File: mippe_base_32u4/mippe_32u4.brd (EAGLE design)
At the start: 160 x 100 mm, 27 parts, among them J2 USB, SW1 BTN-PTS810, U1 ATMEGA32U4-XUMU, U2 AZ1117EH-3.3TRG1, Y1 16MHz

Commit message: Progress on layout
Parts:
- removed C12, C8: 1uF, scono:0603-CAP
- removed U2: AZ1117EH-3.3TRG1, scono:SOT230P700X180-4N
- U1: device SmartPrj:QFN44ML7X7 -> scono:QFN44ML7X7
- Z1, Z2: device varistor:CT/CN0603 -> scono:0603-RES
- moved Y1 130.8 mm to (27.5, 21.8), flipped to the bottom, turned to 270 degrees
- moved C3 129.1 mm to (27.5, 26.8), flipped to the bottom
- moved C4 124.8 mm to (27.8, 17.0), flipped to the bottom
- moved F1 124.4 mm to (13.0, 6.00), turned to 270 degrees
- moved SW1 123.9 mm to (19.2, 32.0), turned to 180 degrees
- moved J2 120.5 mm to (19.2, 2.75)
- moved C1 118.0 mm to (28.5, 22.0), turned to 270 degrees
- moved R2 111.4 mm to (26.2, 17.8), turned to 270 degrees
- moved C2 109.6 mm to (24.0, 10.8), turned to 270 degrees
- moved C5 107.8 mm to (26.2, 22.0), turned to 270 degrees
- moved R1 103.6 mm to (11.8, 26.2), turned to 270 degrees
- moved C11 99.7 mm to (26.8, 8.75), turned to 90 degrees
- moved C6 95.7 mm to (11.8, 17.8), turned to 90 degrees
- moved D1 94.5 mm to (28.8, 3.75), turned to 270 degrees
- moved L3 93.1 mm to (24.5, 6.75), turned to 90 degrees
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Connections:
- removed net 3.3V: C12.2, U2.2, U2.4
- net 5V: no longer C8.2, U2.3
- net GND: no longer C12.1, C8.1, U2.1
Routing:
- net 5V: track 0.00 -> 3.15 mm, vias 0 -> 1
- added copper zone on layer 16, net 5V
- added copper zone on layer 1, net GND

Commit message: blah
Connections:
- net D+ renamed D_P
- net D- renamed D_N
- net RD+ renamed RD_P
- net RD- renamed RD_N
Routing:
- net 5V: track 3.15 -> 29.7 mm, vias 1 -> 11
- net RD_P: track 0.00 -> 7.64 mm
- net RD_N: track 0.00 -> 7.62 mm
- net AGND: track 0.00 -> 7.51 mm
- net D_P: track 0.00 -> 7.20 mm
- net D_N: track 0.00 -> 6.88 mm
- net HWB: track 0.00 -> 6.03 mm
- net AREF: track 0.00 -> 5.01 mm
- net UGND: track 0.00 -> 3.70 mm, vias 0 -> 1
- net UCAP: track 0.00 -> 2.65 mm, vias 0 -> 1

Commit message: layout more
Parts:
- added D2, D3: (no value), scono:LED-0603
- added J1, J4: i2c, scono:1X02
- added J3: spi, scono:1X03
- added J5: BURNIN, scono:BURNIN
- added R3, R7: 330R, scono:0603-RES
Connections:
- new net N$1: D2.C, R3.2
- new net N$2: D3.C, R7.2
- net 5V: now also D2.A, D3.A
- net D0/RX: now also J4.1
- net D1/TX: now also J4.2
- net D2/SDA: now also J1.2
- net D3/SCL: now also J1.1
- net MISO: now also J3.3
- net MOSI: now also J3.2
- net RXLED: now also R7.1
- net SCK: now also J3.1
- net TXLED: now also R3.1
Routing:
- net RESET: track 0.00 -> 27.3 mm, vias 0 -> 2
- net GND: track 0.00 -> 23.6 mm, vias 0 -> 4
- net RXLED: track 0.00 -> 18.9 mm, vias 0 -> 2
- net UGND: track 3.70 -> 21.5 mm
- net SHIELD: track 0.00 -> 16.2 mm
- net SCK: track 0.00 -> 16.0 mm
- net MOSI: track 0.00 -> 14.4 mm
- net D3/SCL: track 0.00 -> 13.1 mm, vias 0 -> 1
- net MISO: track 0.00 -> 13.0 mm
- net D2/SDA: track 0.00 -> 11.6 mm
- net D1/TX: track 0.00 -> 11.1 mm
- net D0/RX: track 0.00 -> 11.0 mm
- net UCAP: track 2.65 -> 12.9 mm
- net XTAL1: track 0.00 -> 9.02 mm, vias 0 -> 1
- net XTAL2: track 0.00 -> 8.61 mm, vias 0 -> 1
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
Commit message: finish 32u4 and rev c burnin
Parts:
- added D4: (no value), scono:LED-0603
- added J6: GND, scono:1X02
- added J7: VCC, scono:1X02
- added R8: 330R, scono:0603-RES
- J4: value i2c -> UART
- moved J1 7.62 mm to (25.4, 17.8)
- moved J3 7.62 mm to (25.4, 10.2)
- moved J4 7.62 mm to (25.4, 22.9)
- moved C1 7.50 mm to (21.0, 22.0)
- moved C11 7.50 mm to (19.2, 8.75)
- moved C2 7.50 mm to (16.5, 10.8)
- moved C3 7.50 mm to (20.0, 26.8)
- moved C4 7.50 mm to (20.2, 17.0)
- moved C5 7.50 mm to (18.8, 22.0)
- moved C6 7.50 mm to (4.25, 17.8)
- moved D2 7.50 mm to (19.3, 32.2)
- moved F1 7.50 mm to (5.50, 6.00)
- moved J2 7.50 mm to (11.8, 2.75)
- moved J5 7.50 mm to (15.5, 32.0)
- moved L2 7.50 mm to (4.25, 14.0)
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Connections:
- new net N$4: D4.C, R8.2
- net 5V: now also J5.3.3V, J7.1, J7.2
- net D7: now also D4.A
- net GND: now also J5.GND, J6.1, J6.2, R8.1
- net MISO: now also J5.MISO
- net MOSI: now also J5.MOSI
- net RESET: now also J5.RST
- net SCK: now also J5.SCK
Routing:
- net SCK: track 16.0 -> 38.2 mm, vias 0 -> 1
- net MISO: track 13.0 -> 33.5 mm, vias 0 -> 1
- net MOSI: track 14.4 -> 33.0 mm, vias 0 -> 1
- net N$3: track 2.01 -> 6.47 mm
- net N$4: track 0.00 -> 3.64 mm
- net D7: track 0.00 -> 3.28 mm
- net RESET: track 27.3 -> 29.8 mm, vias 2 -> 3
- net GND: track 23.6 -> 25.0 mm, vias 4 -> 5
- net 5V: track 33.7 -> 34.5 mm
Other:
- board size 160 x 100 mm -> 28 x 36 mm
- board text added: "Arias Research Group"
- board text added: "Design by Seiya Fa'19"

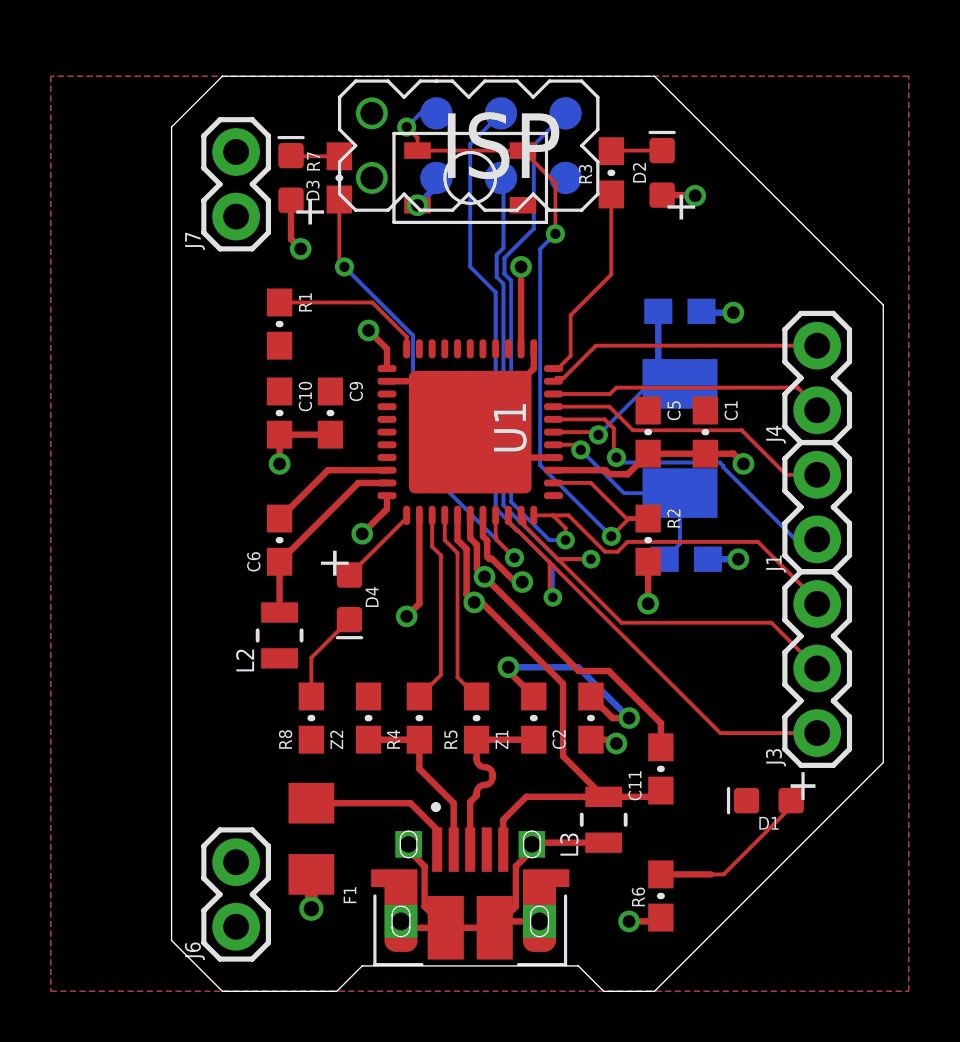
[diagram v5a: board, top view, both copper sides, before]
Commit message: Add same pinpouts as mipp_v2
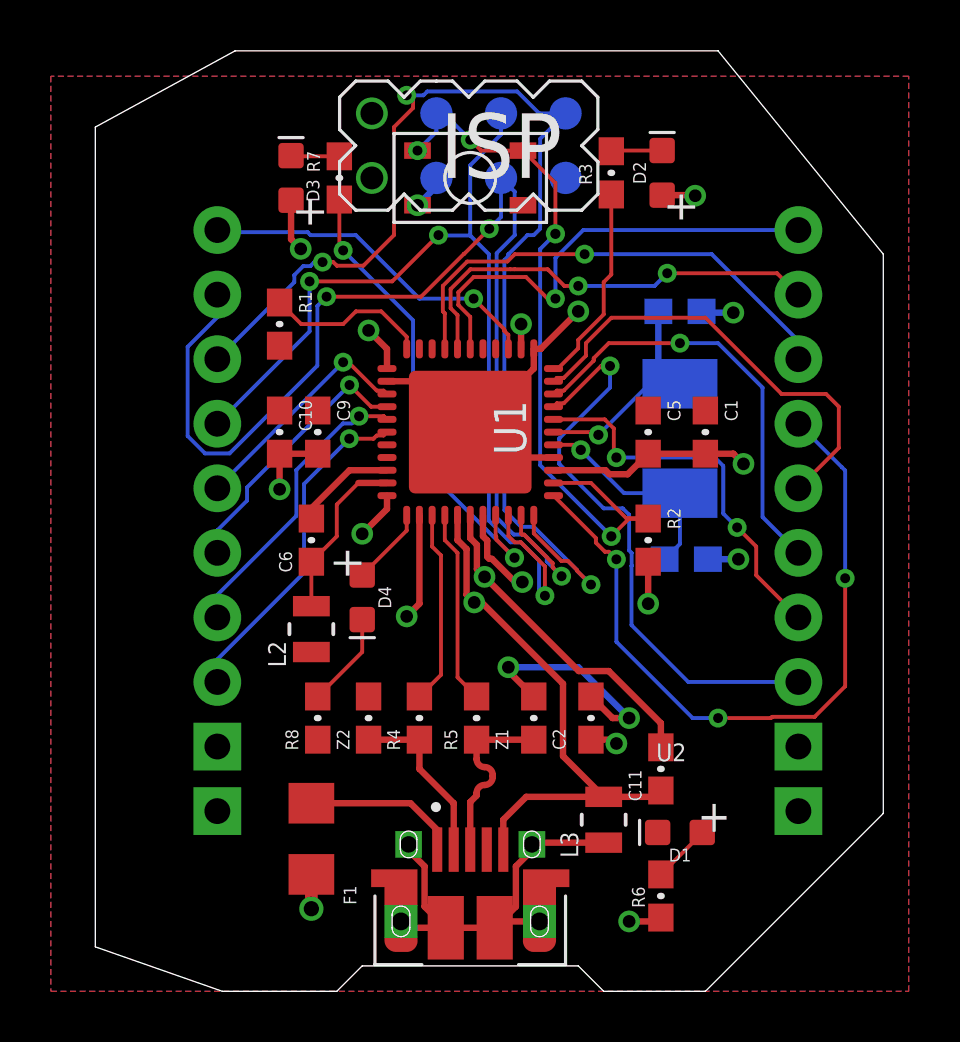
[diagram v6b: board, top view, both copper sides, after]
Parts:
- removed J1: i2c, scono:1X02
- removed J3: spi, scono:1X03
- removed J4: UART, scono:1X02
- removed J6: GND, scono:1X02
- removed J7: VCC, scono:1X02
- added U2: MIPPE, scono:MIPPE
- moved D1 3.72 mm to (20.0, 6.25)
- moved L2 1.27 mm to (5.50, 14.2)
- moved C6 1.25 mm to (5.50, 17.8)
- moved C9 0.90 mm to (5.75, 22.0)
- moved C10 0.75 mm to (4.25, 22.0)
- moved D4 0.50 mm to (7.50, 15.5)
- moved R8 0.25 mm to (5.75, 10.8)
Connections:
- net 5V: now also U2.VCC, U2.VCC@1; no longer J7.1, J7.2
- net A0: now also U2.ADC0
- net A1: now also U2.ADC1
- net A2: now also U2.ADC2
- net A3: now also U2.ADC3
- net D0/RX: now also U2.RX; no longer J4.1
- net D1/TX: now also U2.TX; no longer J4.2
- net D2/SDA: now also U2.SDA; no longer J1.2
- net D3/SCL: now also U2.SCL; no longer J1.1
- net D4: now also U2.SS
- net GND: now also U2.GND@0, U2.GND@1; no longer J6.1, J6.2
- net IO10*: now also U2.GPIO5
- net IO11*: now also U2.GPIO6
- net IO8: now also U2.GPIO3
- net IO9*: now also U2.GPIO4
- net MISO: now also U2.MISO; no longer J3.3
- net MOSI: now also U2.MOSI; no longer J3.2
- net SCK: now also U2.SCK; no longer J3.1
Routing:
- net IO11*: track 0.00 -> 28.7 mm, vias 0 -> 3
- net IO10*: track 0.00 -> 19.1 mm, vias 0 -> 1
- net IO8: track 0.00 -> 18.5 mm, vias 0 -> 1
- net IO9*: track 0.00 -> 17.3 mm, vias 0 -> 2
- net D4: track 0.00 -> 13.7 mm, vias 0 -> 1
- net MISO: track 33.5 -> 47.0 mm, vias 1 -> 3
- net A3: track 0.00 -> 13.3 mm, vias 0 -> 1
- net MOSI: track 33.0 -> 46.0 mm, vias 1 -> 3
- net A2: track 0.00 -> 11.6 mm, vias 0 -> 1
- net D2/SDA: track 11.5 -> 23.0 mm, vias 0 -> 1
- net A1: track 0.00 -> 10.6 mm, vias 0 -> 1
- net A0: track 0.00 -> 9.25 mm, vias 0 -> 1
- net D1/TX: track 11.0 -> 17.9 mm
- net D0/RX: track 10.9 -> 16.9 mm, vias 0 -> 1
- net N$3: track 6.47 -> 2.32 mm
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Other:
- board size 28 x 36 mm -> 31 x 37 mm

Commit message: Add files for jlc order
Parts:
- moved C1 3.00 mm to (24.0, 22.0)
- moved C10 3.00 mm to (7.25, 22.0)
- moved C11 3.00 mm to (22.2, 8.75)
- moved C2 3.00 mm to (19.5, 10.8)
- moved C3 3.00 mm to (23.0, 26.8)
- moved C4 3.00 mm to (23.2, 17.0)
- moved C5 3.00 mm to (21.8, 22.0)
- moved C6 3.00 mm to (8.50, 17.8)
- moved C9 3.00 mm to (8.75, 22.0)
- moved D1 3.00 mm to (23.0, 6.25)
- moved D2 3.00 mm to (22.3, 32.2)
- moved D3 3.00 mm to (7.70, 32.0)
- moved D4 3.00 mm to (10.5, 15.5)
- moved F1 3.00 mm to (8.50, 6.00)
- moved J2 3.00 mm to (14.8, 2.75)
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
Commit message: update jlc drc
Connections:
- removed net UGND: C11.1, J2.5, L3.2, U1.5
- net GND: now also C11.1, J2.5, L3.2, U1.5
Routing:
- net GND: track 27.3 -> 56.2 mm, vias 6 -> 7
- net UGND: track 21.5 -> 0.00 mm, vias 1 -> 0
- net 5V: track 32.0 -> 33.0 mm
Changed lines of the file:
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@@
 <?xml version="1.0" encoding="utf-8"?>
 <!DOCTYPE eagle SYSTEM "eagle.dtd">
-<eagle version="9.5.1">
+<eagle version="9.5.2">
 <drawing>
 <settings>
@@
 </variantdefs>
 <classes>
-<class number="0" name="default" width="0.1524" drill="0.381">
-<clearance class="0" value="0.1524"/>
+<class number="0" name="default" width="0.0889" drill="0.2">
+<clearance class="0" value="0.1397"/>
 </class>
-<class number="1" name="power" width="0.254" drill="0.499">
-<clearance class="0" value="0.1524"/>
-<clearance class="1" value="0.254"/>
-</class>
-<class number="2" name="gnd" width="0.254" drill="0.499">
-<clearance class="0" value="0.1524"/>
+<class number="2" name="gnd" width="0.0889" drill="0.2">
 <clearance class="1" value="0.1524"/>
-<clearance class="2" value="0.254"/>
-</class>
-<class number="3" name="usbvcc" width="0.254" drill="0.499">
-<clearance class="0" value="0.1524"/>
-<clearance class="1" value="0.1524"/>
-<clearance class="2" value="0.1524"/>
-<clearance class="3" value="0.254"/>
-</class>
-<class number="4" name="aref" width="0.254" drill="0.499">
-<clearance class="0" value="0.1524"/>
-<clearance class="1" value="0.1524"/>
-<clearance class="2" value="0.1524"/>
-<clearance class="3" value="0.1524"/>
-<clearance class="4" value="0.254"/>
-</class>
-<class number="5" name="diff pairs" width="0.1524" drill="0">
-<clearance class="0" value="0.1524"/>
-<clearance class="1" value="0.1524"/>
-<clearance class="2" value="0.1524"/>
-<clearance class="3" value="0.1524"/>
-<clearance class="4" value="0.1524"/>
-<clearance class="5" value="0.1524"/>
+<clearance class="2" value="0.1397"/>
 </class>
 </classes>
@@
 </elements>
 <signals>
-<signal name="GND" class="2">
+<signal name="GND">
 <contactref element="U1" pad="15"/>
 <contactref element="U1" pad="23"/>
@@
 <wire x1="17.525" y1="25.275" x2="19" y2="26.75" width="0.254" layer="1"/>
 <via x="19" y="26.75" extent="1-16" drill="0.499"/>
-</signal>
-<signal name="N$3">
-<contactref element="R6" pad="1"/>
-<contactref element="D1" pad="A"/>
-<wire x1="22.25" y1="4.6" x2="23.877" y2="6.227" width="0.1524" layer="1"/>
-<wire x1="23.877" y1="6.227" x2="23.877" y2="6.25" width="0.1524" layer="1"/>
-</signal>
-<signal name="D_N" class="5">
-<contactref element="Z2" pad="1"/>
-<contactref element="R4" pad="1"/>
-<contactref element="J2" pad="2"/>
-<wire x1="10.75" y1="9.9" x2="12.75" y2="9.9" width="0.254" layer="1"/>
-<wire x1="14.1" y1="5.575" x2="14.1" y2="7.4" width="0.254" layer="1"/>
-<wire x1="12.75" y1="8.75" x2="12.75" y2="9.9" width="0.254" layer="1"/>
-<wire x1="12.75" y1="8.75" x2="14.1" y2="7.4" width="0.254" layer="1"/>
-</signal>
-<signal name="D_P" class="5">
-<contactref element="Z1" pad="1"/>
-<contactref element="R5" pad="1"/>
-<contactref element="J2" pad="3"/>
-<wire x1="15" y1="9.9" x2="17.25" y2="9.9" width="0.254" layer="1"/>
-<wire x1="15" y1="9.9" x2="15" y2="9.1393625" width="0.254" layer="1"/>
-<wire x1="15" y1="9.1393625" x2="15.3175" y2="8.8218625" width="0.254" layer="1" curve="90"/>
-<wire x1="15.3175" y1="8.8218625" x2="15.635" y2="8.5043625" width="0.254" layer="1" curve="-90"/>
-<wire x1="15.635" y1="8.5043625" x2="15.635" y2="8.435" width="0.254" layer="1"/>
-<wire x1="15.635" y1="8.435" x2="15.3175" y2="8.1175" width="0.254" layer="1" curve="-90"/>
-<wire x1="15.3175" y1="8.1175" x2="15" y2="7.8" width="0.254" layer="1" curve="90"/>
-<wire x1="15" y1="7.8" x2="15" y2="7.7" width="0.254" layer="1"/>
-<wire x1="14.75" y1="5.575" x2="14.75" y2="7.45" width="0.254" layer="1"/>
-<wire x1="15" y1="7.7" x2="14.75" y2="7.45" width="0.254" layer="1"/>
-</signal>
-<signal name="UGND" class="2">
 <contactref element="U1" pad="5"/>
 <contactref element="C11" pad="1"/>
@@
 <wire x1="18.4" y1="12.1" x2="15.2" y2="15.3" width="0.254" layer="1"/>
 <wire x1="15.2" y1="15.3" x2="14.9059" y2="15.3" width="0.254" layer="1"/>
+<wire x1="22.25" y1="7.9" x2="22.25" y2="6.377" width="0.254" layer="1"/>
+<wire x1="22.25" y1="6.377" x2="22.123" y2="6.25" width="0.254" layer="1"/>
+<wire x1="22.25" y1="7.9" x2="22.4" y2="7.75" width="0.254" layer="1"/>
+<wire x1="27" y1="7.75" x2="27.66" y2="7.09" width="0.254" layer="1"/>
+<wire x1="22.4" y1="7.75" x2="27" y2="7.75" width="0.254" layer="1"/>
+<wire x1="24" y1="22.85" x2="23.85" y2="26.75" width="0" layer="19" extent="1-16"/>
+<wire x1="21.75" y1="22.85" x2="24" y2="22.85" width="0" layer="19" extent="1-1"/>
+<wire x1="18.025" y1="21" x2="21.75" y2="22.85" width="0" layer="19" extent="1-1"/>
+<wire x1="8.75" y1="22.85" x2="11.475" y2="24" width="0" layer="19" extent="1-1"/>
+<wire x1="7.25" y1="22.85" x2="8.75" y2="22.85" width="0" layer="19" extent="1-1"/>
+<wire x1="7.25" y1="25.4" x2="7.25" y2="22.85" width="0" layer="19" extent="1-1"/>
+<wire x1="14.25" y1="18.725" x2="14.75" y2="22" width="0" layer="19" extent="1-1"/>
+<wire x1="27.66" y1="9.63" x2="27.66" y2="7.09" width="0" layer="19" extent="1-1"/>
+<wire x1="16.25" y1="12.75" x2="14.9059" y2="15.3" width="0" layer="19" extent="1-1"/>
+<wire x1="16.825" y1="30.925" x2="19" y2="26.75" width="0" layer="19" extent="1-1"/>
+<wire x1="13.42" y1="32" x2="16.825" y2="30.925" width="0" layer="19" extent="1-16"/>
+<wire x1="10.75" y1="11.6" x2="14.9059" y2="15.3" width="0" layer="19" extent="1-1"/>
+<wire x1="8.75" y1="9.9" x2="10.75" y2="11.6" width="0" layer="19" extent="1-1"/>
+<wire x1="8.5" y1="13.3484" x2="10.75" y2="11.6" width="0" layer="19" extent="1-1"/>
+<wire x1="24.1" y1="17" x2="24" y2="22.85" width="0" layer="19" extent="1-16"/>
+</signal>
+<signal name="N$3">
+<contactref element="R6" pad="1"/>
+<contactref element="D1" pad="A"/>
+<wire x1="22.25" y1="4.6" x2="23.877" y2="6.227" width="0.1524" layer="1"/>
+<wire x1="23.877" y1="6.227" x2="23.877" y2="6.25" width="0.1524" layer="1"/>
+</signal>
+<signal name="D_N">
+<contactref element="Z2" pad="1"/>
+<contactref element="R4" pad="1"/>
+<contactref element="J2" pad="2"/>
+<wire x1="10.75" y1="9.9" x2="12.75" y2="9.9" width="0.254" layer="1"/>
+<wire x1="14.1" y1="5.575" x2="14.1" y2="7.4" width="0.254" layer="1"/>
+<wire x1="12.75" y1="8.75" x2="12.75" y2="9.9" width="0.254" layer="1"/>
+<wire x1="12.75" y1="8.75" x2="14.1" y2="7.4" width="0.254" layer="1"/>
+</signal>
+<signal name="D_P">
+<contactref element="Z1" pad="1"/>
+<contactref element="R5" pad="1"/>
+<contactref element="J2" pad="3"/>
+<wire x1="15" y1="9.9" x2="17.25" y2="9.9" width="0.254" layer="1"/>
+<wire x1="15" y1="9.9" x2="15" y2="9.1393625" width="0.254" layer="1"/>
+<wire x1="15" y1="9.1393625" x2="15.3175" y2="8.8218625" width="0.254" layer="1" curve="90"/>
+<wire x1="15.3175" y1="8.8218625" x2="15.635" y2="8.5043625" width="0.254" layer="1" curve="-90"/>
+<wire x1="15.635" y1="8.5043625" x2="15.635" y2="8.435" width="0.254" layer="1"/>
+<wire x1="15.635" y1="8.435" x2="15.3175" y2="8.1175" width="0.254" layer="1" curve="-90"/>
+<wire x1="15.3175" y1="8.1175" x2="15" y2="7.8" width="0.254" layer="1" curve="90"/>
+<wire x1="15" y1="7.8" x2="15" y2="7.7" width="0.254" layer="1"/>
+<wire x1="14.75" y1="5.575" x2="14.75" y2="7.45" width="0.254" layer="1"/>
+<wire x1="15" y1="7.7" x2="14.75" y2="7.45" width="0.254" layer="1"/>
 </signal>
 <signal name="XUSB">
@@
 <wire x1="13.45" y1="6.35" x2="12.4" y2="7.4" width="0.254" layer="1"/>
 </signal>
-<signal name="AREF" class="4">
+<signal name="AREF">
 <contactref element="U1" pad="42"/>
 <contactref element="C6" pad="2"/>
@@
 <wire x1="20" y1="26.62965625" x2="20" y2="27.9" width="0.1524" layer="1"/>
 </signal>
-<signal name="5V" class="1">
+<signal name="5V">
 <contactref element="U1" pad="7"/>
 <contactref element="C10" pad="2"/>
@@
 <wire x1="7.25" y1="21.15" x2="7.25" y2="19.75" width="0.254" layer="1"/>
 <via x="7.25" y="19.75" extent="1-16" drill="0.499"/>
-<wire x1="16.75" y1="25.275" x2="16.75" y2="26.25" width="0.254" layer="1"/>
-<via x="16.75" y="26.25" extent="1-16" drill="0.499"/>
+<wire x1="16.75" y1="25.275" x2="16.75" y2="27.25" width="0.254" layer="1"/>
+<via x="16.75" y="27.25" extent="1-16" drill="0.499"/>
+<wire x1="18.5" y1="32" x2="22.3" y2="31.323" width="0" layer="19" extent="1-16"/>
+<wire x1="16.75" y1="27.25" x2="18.5" y2="32" width="0" layer="19" extent="16-16"/>
+<wire x1="18.025" y1="20.5" x2="16.75" y2="25.275" width="0" layer="19" extent="1-1"/>
+<wire x1="15.25" y1="18.725" x2="18.025" y2="20.5" width="0" layer="19" extent="1-1"/>
+<wire x1="12.75" y1="18.725" x2="15.25" y2="18.725" width="0" layer="19" extent="1-1"/>
+<wire x1="11.475" y1="19.5" x2="12.75" y2="18.725" width="0" layer="19" extent="1-1"/>
+<wire x1="8.75" y1="21.15" x2="11.475" y2="19.5" width="0" layer="19" extent="1-1"/>
+<wire x1="21.75" y1="16.9" x2="21.75" y2="21.15" width="0" layer="19" extent="1-1"/>
+<wire x1="11.475" y1="24.5" x2="8.75" y2="21.15" width="0" layer="19" extent="1-1"/>
+<wire x1="8.08" y1="29.21" x2="10.75" y2="26" width="0" layer="19" extent="1-1"/>
+<wire x1="20.5" y1="9.75" x2="21.75" y2="15.25" width="0" layer="19" extent="1-1"/>
+<wire x1="21" y1="2.75" x2="20.5" y2="9.75" width="0" layer="19" extent="1-1"/>
+<wire x1="4.8" y1="9.63" x2="12.25" y2="14.75" width="0" layer="19" extent="1-1"/>
+<wire x1="4.8" y1="7.09" x2="4.8" y2="9.63" width="0" layer="19" extent="1-1"/>
+<wire x1="8.5" y1="4.6" x2="4.8" y2="7.09" width="0" layer="19" extent="1-1"/>
 </signal>
 <signal name="USBID">
@@
 <wire x1="17.2434" y1="5.8484" x2="17.175" y2="5.78" width="0.254" layer="1"/>
 </signal>
-<signal name="RD_N" class="5">
+<signal name="RD_N">
 <contactref element="U1" pad="3"/>
 <contactref element="R4" pad="2"/>
@@
 <wire x1="13.6" y1="12.45" x2="12.75" y2="11.6" width="0.1524" layer="1"/>
 </signal>
-<signal name="RD_P" class="5">
+<signal name="RD_P">
 <contactref element="U1" pad="4"/>
 <contactref element="R5" pad="2"/>
